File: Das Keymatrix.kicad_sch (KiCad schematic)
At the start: 0 parts

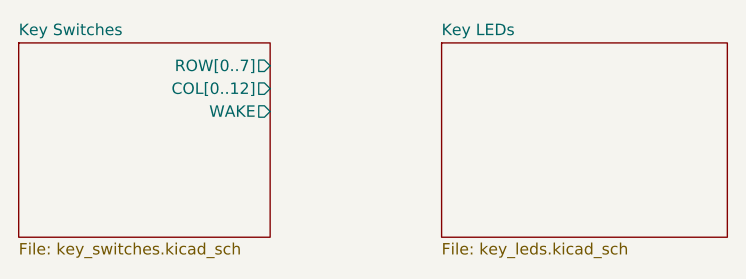
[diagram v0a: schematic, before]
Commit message: Add power connections to LED sheet
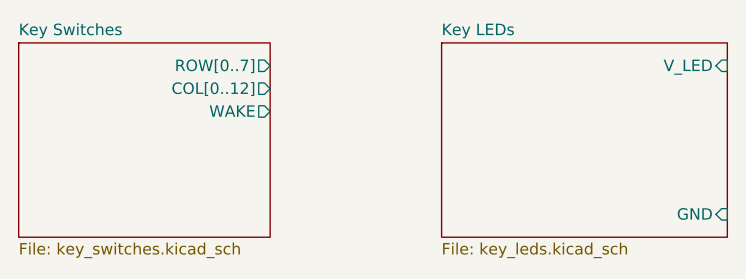
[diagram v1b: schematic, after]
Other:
- sheet Key LEDs ports: added GND, V_LED; removed none
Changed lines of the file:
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@@
       (effects (font (size 1.27 1.27)) (justify left top))
+    )
+    (pin "GND" input (at 154.94 100.33 0)
+      (effects (font (size 1.27 1.27)) (justify right))
+    )
+    (pin "V_LED" input (at 154.94 83.82 0)
+      (effects (font (size 1.27 1.27)) (justify right))
     )
     (instances
